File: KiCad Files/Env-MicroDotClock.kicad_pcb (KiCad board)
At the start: 2 copper layers, 90 x 65.2 mm, 40 parts, among them IC1 IS31FL3730-QFLS2-TR, IC2 IS31FL3730-QFLS2-TR, IC3 IS31FL3730-QFLS2-TR, IC4 IS31FL3730-QFLS2-TR, M1 Dip-14 Socket, M2 Dip-14 Socket, M3 Dip-14 Socket, M4 Dip-14 Socket, M5 Dip-14 Socket, M6 Dip-14 Socket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

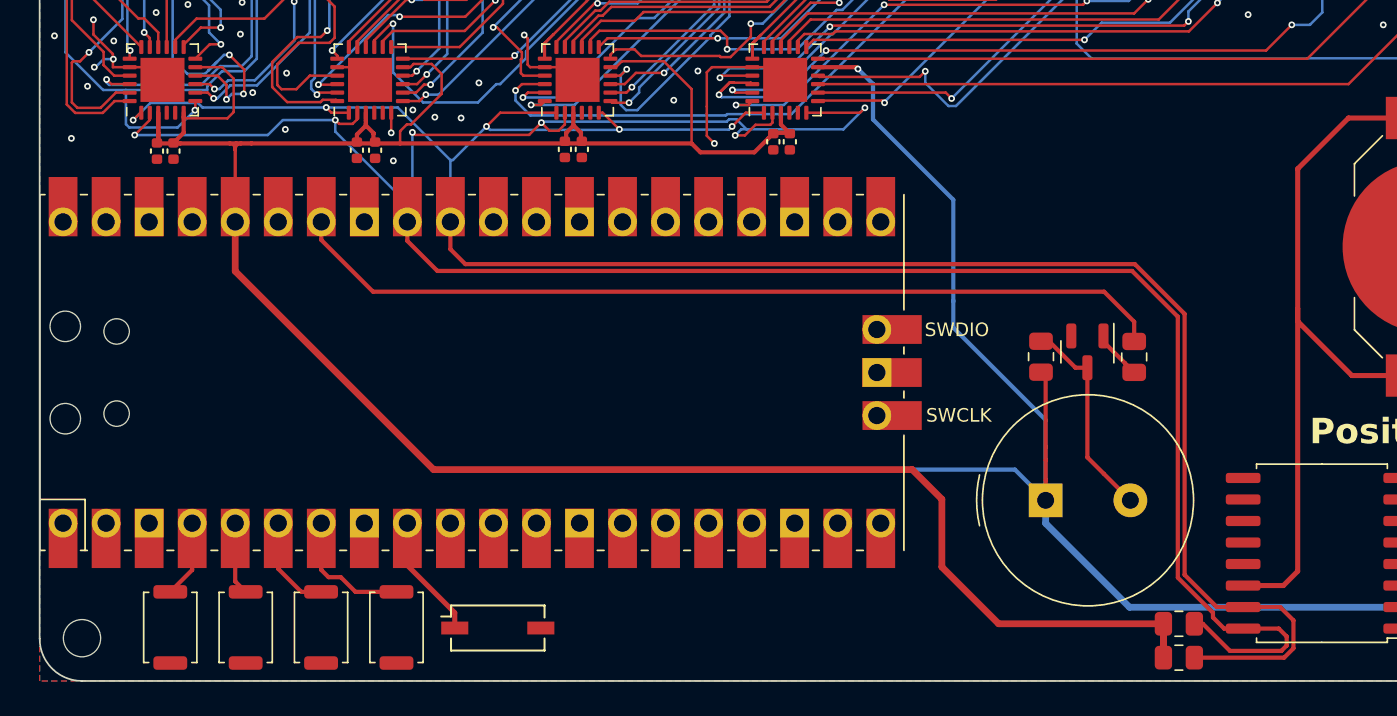
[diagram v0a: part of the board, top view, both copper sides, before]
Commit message: moved all i2c devices to dedicated gpio pairs, added individual pullups, ensured everything is 3.3V VCC or logic level 3V3 tied
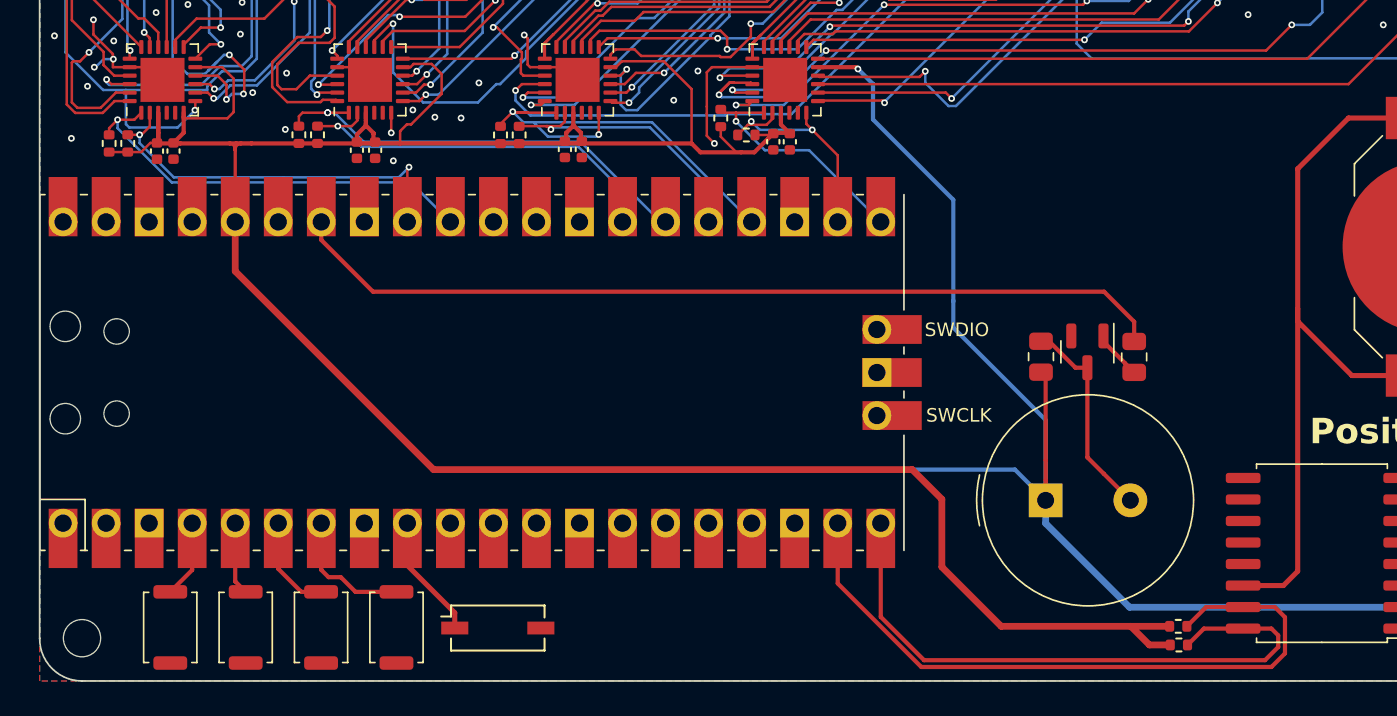
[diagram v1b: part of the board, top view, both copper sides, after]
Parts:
- added R10: 0402 10K, Resistor_SMD:R_0402_1005Metric, F.Cu at (90.2, 91.0)
- added R11: 0402 10K, Resistor_SMD:R_0402_1005Metric, F.Cu at (100.3, 90.5)
- added R12: 0402 10K, Resistor_SMD:R_0402_1005Metric, F.Cu at (101.4, 90.5)
- added R5: 0402 10K, Resistor_SMD:R_0402_1005Metric, F.Cu at (125.2, 89.5)
- added R6: 0402 10K, Resistor_SMD:R_0402_1005Metric, F.Cu at (126.7, 90.5)
- added R7: 0402 10K, Resistor_SMD:R_0402_1005Metric, F.Cu at (112.2, 90.5)
- added R8: 0402 10K, Resistor_SMD:R_0402_1005Metric, F.Cu at (113.3, 90.5)
- added R9: 0402 10K, Resistor_SMD:R_0402_1005Metric, F.Cu at (89.1, 91.0)
- R1, R2: value 0805 10K -> 0402 10K; footprint Resistor_SMD:R_0805_2012Metric -> Resistor_SMD:R_0402_1005Metric
- moved R2 1.85 mm to (152.2, 119.5)
- moved R1 1.25 mm to (152.2, 120.6)
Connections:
- IC1 pad 1: I2C_SDA -> I2C1_SDA
- IC1 pad 2: I2C_SCL -> I2C1_SCL
- IC2 pad 1: I2C_SDA -> I2C2_SDA
- IC2 pad 2: I2C_SCL -> I2C2_SCL
- IC3 pad 1: I2C_SDA -> I2C3_SDA
- IC3 pad 2: I2C_SCL -> I2C3_SCL
- IC3 pad 6: I2C_SDA -> I2C3_SDA
- IC4 pad 1: I2C_SDA -> I2C4_SDA
- IC4 pad 2: I2C_SCL -> I2C4_SCL
- IC4 pad 6: I2C_SCL -> I2C4_SCL
- R1 pad 2: I2C_SCL -> RTC_SCL
- R2 pad 2: I2C_SDA -> RTC_SDA
- U1 pad 19: unconnected-(U1-GPIO14-Pad19) -> RTC_SDA
- U1 pad 20: unconnected-(U1-GPIO15-Pad20) -> RTC_SCL
- U1 pad 21: unconnected-(U1-GPIO16-Pad21) -> I2C4_SDA
- U1 pad 22: unconnected-(U1-GPIO17-Pad22) -> I2C4_SCL
- U1 pad 24: unconnected-(U1-GPIO18-Pad24) -> I2C3_SDA
- U1 pad 25: unconnected-(U1-GPIO19-Pad25) -> I2C3_SCL
- U1 pad 26: unconnected-(U1-GPIO20-Pad26) -> I2C2_SDA
- U1 pad 27: unconnected-(U1-GPIO21-Pad27) -> I2C2_SCL
- U1 pad 31: I2C_SDA -> I2C1_SDA
- U1 pad 32: I2C_SCL -> I2C1_SCL
- U3 pad 15: I2C_SDA -> RTC_SDA
- U3 pad 16: I2C_SCL -> RTC_SCL
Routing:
- net I2C_SCL: track 145.0 -> 0.00 mm, vias 6 -> 0
- net I2C_SDA: track 131.3 -> 0.00 mm, vias 5 -> 0
- net RTC_SDA: track 0.00 -> 41.0 mm
- net RTC_SCL: track 0.00 -> 37.0 mm
- net I2C3_SDA: track 0.00 -> 27.0 mm, vias 0 -> 2
- net I2C2_SDA: track 0.00 -> 26.2 mm, vias 0 -> 2
- net I2C1_SDA: track 0.00 -> 25.1 mm, vias 0 -> 1
- net I2C2_SCL: track 0.00 -> 23.2 mm, vias 0 -> 1
- net I2C1_SCL: track 0.00 -> 23.1 mm, vias 0 -> 2
- net I2C3_SCL: track 0.00 -> 16.6 mm, vias 0 -> 1
- net I2C4_SDA: track 0.00 -> 14.1 mm, vias 0 -> 1
- net I2C4_SCL: track 0.00 -> 14.0 mm, vias 0 -> 2
- net +3V3: track 293.7 -> 298.9 mm

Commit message: changes toward a V2, replaced battery holder with larger one, moved rtc leftward to make space for larger battery.
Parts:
- removed SW5: DIP SPST W5.08mm_P1.27mm, Button_Switch_SMD:SW_DIP_SPSTx01_Slide_Copal_CHS-01A_W5.08mm_P1.27mm_JPin
- added REF**: KiCad-Logo2_6mm_SilkScreen, Symbol:KiCad-Logo2_6mm_SilkScreen, B.Cu at (124.0, 104.5)
- BT1: value HLD-012 -> Keystone 3034; footprint Battery:BatteryHolder_LINX_BAT-HLD-012-SMT -> Battery:BatteryHolder_Keystone_3034_1x20mm
- moved BZ1 17.3 mm to (147.0, 95.0), turned to 180 degrees
- moved C10 16.0 mm to (152.2, 117.9)
- moved C9 16.0 mm to (151.2, 117.9)
- moved R1 16.0 mm to (136.2, 120.6)
- moved R2 16.0 mm to (136.2, 119.5)
- moved U3 16.0 mm to (144.7, 115.2)
- moved BT1 8.47 mm to (161.8, 103.8)
- moved R4 7.83 mm to (141.8, 103.5), turned to 90 degrees
- moved R3 3.18 mm to (147.3, 103.5), turned to -90 degrees
- moved Q1 2.35 mm to (144.5, 103.8), turned to 90 degrees
- moved R6 1.51 mm to (125.2, 90.4), turned to 90 degrees
- moved R5 1.42 mm to (124.1, 90.4)
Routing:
- net +3V3: track 298.9 -> 271.5 mm, vias 2 -> 3
- net RTC_SCL: track 37.0 -> 22.3 mm
- net RTC_SDA: track 41.0 -> 26.7 mm
- net Net-(BT1-+): track 46.1 -> 55.7 mm
- net GPIO6: track 7.35 -> 0.00 mm
- net Buzzer GPIO: track 52.8 -> 46.9 mm
- net IC4C2: track 63.6 -> 65.7 mm
- net I2C4_SDA: track 14.1 -> 15.5 mm
- net I2C4_SCL: track 14.0 -> 14.9 mm
- net IC4C5: track 67.2 -> 66.4 mm
- net IC4R5: track 59.5 -> 60.1 mm
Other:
- board text added: "CR20XX"
- board text removed: "CR1220"

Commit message: small tweaks + generated production files
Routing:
- net IC3C5: track 52.3 -> 50.6 mm
- net Net-(BT1-+): track 55.7 -> 54.5 mm
- net Buzzer GPIO: track 46.9 -> 45.9 mm
- net IC4C5: track 66.4 -> 65.5 mm
- net I2C2_SDA: vias 2 -> 1
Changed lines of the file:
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@@
   (segment (start 139.2 72.845) (end 136.309 72.845) (width 0.15) (layer "F.Cu") (net 46))
   (segment (start 119 85.45) (end 120.1128 85.45) (width 0.15) (layer "F.Cu") (net 46))
-  (segment (start 118.6875 85.9999) (end 118.6875 86) (width 0.15) (layer "F.Cu") (net 46))
   (segment (start 136.309 72.845) (end 134.903 74.2513) (width 0.15) (layer "F.Cu") (net 46))
   (segment (start 120.1128 85.45) (end 120.5 85.8372) (width 0.15) (layer "F.Cu") (net 46))
@@
   (segment (start 138.810736 67.765) (end 139.2 67.765) (width 0.15) (layer "F.Cu") (net 53))
   (segment (start 149.595 72.845) (end 143.25 66.5) (width 0.15) (layer "F.Cu") (net 53))
-  (segment (start 114.8125 86) (end 114.8125 85.079218) (width 0.15) (layer "F.Cu") (net 53))
   (segment (start 116.933007 82.2129) (end 114.8125 84.333407) (width 0.15) (layer "F.Cu") (net 53))
   (segment (start 114.8125 84.333407) (end 114.8125 86) (width 0.15) (layer "F.Cu") (net 53))
   (segment (start 121.9476 82.2129) (end 116.933007 82.2129) (width 0.15) (layer "F.Cu") (net 53))
   (segment (start 143.25 66.5) (end 141.5658 66.5) (width 0.15) (layer "F.Cu") (net 53))
-  (segment (start 114.812 85.3097) (end 114.8125 85.3102) (width 0.15) (layer "F.Cu") (net 53))
   (segment (start 132.450736 74.125) (end 138.810736 67.765) (width 0.15) (layer "F.Cu") (net 53))
-  (segment (start 114.8125 85.3102) (end 114.8125 86) (width 0.15) (layer "F.Cu") (net 53))
   (segment (start 121.95 82.2153) (end 121.9476 82.2129) (width 0.15) (layer "F.Cu") (net 53))
   (segment (start 141.5658 66.5) (end 140.3008 67.765) (width 0.15) (layer "F.Cu") (net 53))
@@
   (segment (start 141.3205 82.2161) (end 141.6694 81.8672) (width 0.15) (layer "F.Cu") (net 71))
   (segment (start 150.337695 81.5612) (end 151.3888 81.5612) (width 0.15) (layer "F.Cu") (net 71))
-  (segment (start 127.0625 86) (end 127.0625 85.107006) (width 0.15) (layer "F.Cu") (net 71))
   (segment (start 153.5203 76.675) (end 158.5085 71.6868) (width 0.15) (layer "F.Cu") (net 71))
   (segment (start 160.7 67.765) (end 161.865 66.6) (width 0.15) (layer "F.Cu") (net 71))
@@
   (via (at 106.8 92.4) (size 0.4) (drill 0.2) (layers "F.Cu" "B.Cu") (net 84))
   (via (at 90.9 90.49) (size 0.4) (drill 0.2) (layers "F.Cu" "B.Cu") (net 84))
-  (segment (start 99.4 93) (end 92.924264 93) (width 0.15) (layer "B.Cu") (net 84))
+  (segment (start 92.924264 93) (end 106.2 93) (width 0.15) (layer "B.Cu") (net 84))
   (segment (start 106.2 93) (end 106.8 92.4) (width 0.15) (layer "B.Cu") (net 84))
   (segment (start 90.9 90.975736) (end 90.9 90.49) (width 0.15) (layer "B.Cu") (net 84))
-  (segment (start 99.4 93) (end 106.2 93) (width 0.15) (layer "B.Cu") (net 84))
   (segment (start 92.924264 93) (end 90.9 90.975736) (width 0.15) (layer "B.Cu") (net 84))
   (segment (start 100.5125 89.1875) (end 100.3 89.4) (width 0.15) (layer "F.Cu") (net 85))
   (segment (start 100.3 89.4) (end 100.3 89.98) (width 0.15) (layer "F.Cu") (net 85))
   (segment (start 103.25 89.1875) (end 100.5125 89.1875) (width 0.15) (layer "F.Cu") (net 85))
-  (via (at 102 89.1875) (size 0.4) (drill 0.2) (layers "F.Cu" "B.Cu") (net 85))
   (via (at 102 89.1875) (size 0.4) (drill 0.2) (layers "F.Cu" "B.Cu") (net 85))
   (segment (start 102.0125 89.2) (end 102 89.1875) (width 0.15) (layer "B.Cu") (net 85))
@@
   (segment (start 91.925 91) (end 92 91) (width 0.25) (layer "F.Cu") (net 95))
   (segment (start 104.25 89.8254) (end 104.25 89.65) (width 0.25) (layer "F.Cu") (net 95))
-  (segment (start 128.22 90.5) (end 128.3 90.42) (width 0.15) (layer "F.Cu") (net 95))
   (segment (start 128.0053 90.6997) (end 128.0203 90.6997) (width 0.15) (layer "F.Cu") (net 95))
   (segment (start 116.95 90.87) (end 116.95 91) (width 0.25) (layer "F.Cu") (net 95))
@@
   (segment (start 96.5424 95.631) (end 96.5424 91.375) (width 0.2) (layer "F.Cu") (net 95))
   (segment (start 92.9 90.97) (end 93.5 90.37) (width 0.25) (layer "F.Cu") (net 95))
-  (segment (start 146.9997 94.9999) (end 146.9997 94.9998) (width 0.15) (layer "F.Cu") (net 95))
   (segment (start 119.01 86.5) (end 119.36 86.1501) (width 0.15) (layer "F.Cu") (net 95))
   (segment (start 118.688 86.5) (end 119.01 86.5) (width 0.15) (layer "F.Cu") (net 95))
@@
   (segment (start 116.5 89.925) (end 116.95 90.375) (width 0.25) (layer "F.Cu") (net 95))
   (segment (start 93.5736 89.5187) (end 96.0813 89.5187) (width 0.15) (layer "F.Cu") (net 95))
-  (segment (start 135.7275 119.4625) (end 135.69 119.5) (width 0.4) (layer "F.Cu") (net 95))
   (segment (start 103.725 91) (end 104.7 91) (width 0.25) (layer "F.Cu") (net 95))
   (segment (start 106.275 90.275) (end 106.675 89.875) (width 0.15) (layer "F.Cu") (net 95))
@@
   (segment (start 135.69 118.81) (end 135.69 119.5) (width 0.4) (layer "F.Cu") (net 95))
   (segment (start 93.5 89.4451) (end 93.5 89.1875) (width 0.25) (layer "F.Cu") (net 95))
-  (segment (start 146.9997 94.9998) (end 146.9997 94.9999) (width 0.25) (layer "F.Cu") (net 95))
   (segment (start 124.1 90.91) (end 125.2 90.91) (width 0.25) (layer "F.Cu") (net 95))
   (segment (start 127.795 90.91) (end 128.0053 90.6997) (width 0.25) (layer "F.Cu") (net 95))
@@
   (segment (start 135.25 110.25) (end 108.2 110.25) (width 0.4) (layer "B.Cu") (net 95))
   (segment (start 144 112) (end 144 115.5) (width 0.6) (layer "F.Cu") (net 101))
-  (segment (start 151.25 98.25) (end 149.75 99.75) (width 0.6) (layer "F.Cu") (net 101))
-  (segment (start 144 115.5) (end 142.406 117.094) (width 0.6) (layer "F.Cu") (net 101))
+  (segment (start 149.75 99.75) (end 156.735 92.765) (width 0.6) (layer "F.Cu") (net 101))
+  (segment (start 142.406 117.094) (end 144 115.5) (width 0.6) (layer "F.Cu") (net 101))
   (segment (start 150.25 108.5) (end 156.485 114.735) (width 0.6) (layer "F.Cu") (net 101))
-  (segment (start 145.25 110.75) (end 144 112) (width 0.6) (layer "F.Cu") (net 101))
-  (segment (start 149.75 104.75) (end 149.75 106.25) (width 0.6) (layer "F.Cu") (net 101))
-  (segment (start 156.735 92.765) (end 151.25 98.25) (width 0.6) (layer "F.Cu") (net 101))
+  (segment (start 144 112) (end 147.5 108.5) (width 0.6) (layer "F.Cu") (net 101))
+  (segment (start 149.75 99.75) (end 149.75 106.25) (width 0.6) (layer "F.Cu") (net 101))
   (segment (start 149.75 106.25) (end 147.5 108.5) (width 0.6) (layer "F.Cu") (net 101))
   (segment (start 147.5 108.5) (end 150.25 108.5) (width 0.6) (layer "F.Cu") (net 101))
-  (segment (start 149.75 99.75) (end 149.75 104.75) (width 0.6) (layer "F.Cu") (net 101))
   (segment (start 142.406 117.094) (end 140.0304 117.094) (width 0.6) (layer "F.Cu") (net 101))
-  (segment (start 142.406 117.094) (end 143.25 116.25) (width 0.6) (layer "F.Cu") (net 101))
   (segment (start 156.485 114.735) (end 161.75 114.735) (width 0.6) (layer "F.Cu") (net 101))
-  (segment (start 147.5 108.5) (end 145.25 110.75) (width 0.6) (layer "F.Cu") (net 101))
   (segment (start 161.75 92.765) (end 156.735 92.765) (width 0.6) (layer "F.Cu") (net 101))
   (segment (start 142.0457 102.8228) (end 141.7737 102.5508) (width 0.25) (layer "F.Cu") (net 103))
@@
   (segment (start 143.5867 104.6956) (end 143.5867 104.6982) (width 0.15) (layer "F.Cu") (net 103))
   (segment (start 143.5867 104.6588) (end 143.5867 104.6798) (width 0.15) (layer "F.Cu") (net 103))
-  (segment (start 101.622 95.6643) (end 101.622 95.6476) (width 0.15) (layer "F.Cu") (net 104))
   (segment (start 101.622 95.6476) (end 101.622 95.631) (width 0.15) (layer "F.Cu") (net 104))
   (segment (start 131.5 99) (end 131 98.5) (width 0.4) (layer "F.Cu") (net 104))
-  (segment (start 101.622 95.8974) (end 101.622 95.7642) (width 0.15) (layer "F.Cu") (net 104))
   (segment (start 137 99) (end 131.5 99) (width 0.4) (layer "F.Cu") (net 104))
-  (segment (start 101.622 95.7642) (end 101.622 95.6976) (width 0.15) (layer "F.Cu") (net 104))
-  (segment (start 101.622 95.6643) (end 101.622 95.6476) (width 0.25) (layer "F.Cu") (net 104))
   (segment (start 101.622 95.6476) (end 101.622 95.631) (width 0.25) (layer "F.Cu") (net 104))
-  (segment (start 101.622 96.1642) (end 101.622 96.1638) (width 0.15) (layer "F.Cu") (net 104))
   (segment (start 102.5 98.5) (end 101.6224 97.6224) (width 0.4) (layer "F.Cu") (net 104))
   (segment (start 101.6224 97.6224) (end 101.6224 95.631) (width 0.4) (layer "F.Cu") (net 104))
-  (segment (start 101.622 96.1642) (end 101.622 96.1638) (width 0.25) (layer "F.Cu") (net 104))
   (segment (start 139 102.5) (end 139 101) (width 0.4) (layer "F.Cu") (net 104))
   (segment (start 101.622 95.6476) (end 101.6224 95.6472) (width 0.15) (layer "F.Cu") (net 104))
   (segment (start 140.8753 104.3753) (end 139 102.5) (width 0.4) (layer "F.Cu") (net 104))
-  (segment (start 101.622 95.7642) (end 101.622 95.6976) (width 0.25) (layer "F.Cu") (net 104))
   (segment (start 131 98.5) (end 102.5 98.5) (width 0.4) (layer "F.Cu") (net 104))
-  (segment (start 101.622 95.6976) (end 101.622 95.6643) (width 0.15) (layer "F.Cu") (net 104))
-  (segment (start 101.622 95.8974) (end 101.622 95.7642) (width 0.25) (layer "F.Cu") (net 104))
-  (segment (start 101.622 96.1638) (end 101.622 95.8974) (width 0.15) (layer "F.Cu") (net 104))
   (segment (start 141.7737 104.3753) (end 140.8753 104.3753) (width 0.4) (layer "F.Cu") (net 104))
-  (segment (start 101.622 96.1638) (end 101.622 95.8974) (width 0.25) (layer "F.Cu") (net 104))
   (segment (start 139 101) (end 137 99) (width 0.4) (layer "F.Cu") (net 104))
-  (segment (start 101.622 95.6976) (end 101.622 95.6643) (width 0.25) (layer "F.Cu") (net 104))
   (segment (start 101.6224 95.6472) (end 101.6224 95.631) (width 0.15) (layer "F.Cu") (net 104))
   (segment (start 142.5 118.964) (end 142.5 121.1) (width 0.25) (layer "F.Cu") (net 105))

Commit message: removed all traces for work on future version
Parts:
- removed REF**: KiCad-Logo2_6mm_SilkScreen, Symbol:KiCad-Logo2_6mm_SilkScreen
- IC1, IC2, IC3, IC4: footprint Package_DFN_QFN:QFN-24-1EP_4x4mm_P0.5mm_EP2.6x2.6mm -> Package_DFN_QFN:QFN-24-1EP_4x4mm_P0.5mm_EP2.6x2.6mm_ThermalVias
- moved R5 9.80 mm to (131.2, 83.6), turned to -90 degrees
- moved R7 9.71 mm to (118.9, 83.5), turned to -90 degrees
- moved R11 9.39 mm to (106.7, 83.6), turned to -90 degrees
- moved R9 9.09 mm to (94.3, 83.5), turned to -90 degrees
- moved R6 8.36 mm to (130.1, 83.6), turned to -90 degrees
- moved R8 8.34 mm to (117.8, 83.5), turned to -90 degrees
- moved R12 8.06 mm to (105.5, 83.6), turned to -90 degrees
- moved R10 8.03 mm to (93.2, 83.5), turned to -90 degrees
- moved C2 5.80 mm to (87.7, 89.0), turned to 180 degrees
- moved C1 5.49 mm to (87.7, 88.0), turned to 180 degrees
- moved C4 5.15 mm to (100.2, 89.1), turned to 180 degrees
- moved C6 5.13 mm to (112.4, 89.0), turned to 180 degrees
- moved C8 4.99 mm to (124.7, 89.0), turned to 180 degrees
- moved C3 4.90 mm to (100.2, 88.0), turned to 180 degrees
- moved C5 4.88 mm to (112.4, 88.0), turned to 180 degrees
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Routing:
- net +3V3: track 271.3 -> 0.00 mm, vias 3 -> 0
- net IC4R3: track 66.2 -> 0.00 mm
- net IC4C2: track 65.7 -> 0.00 mm, vias 1 -> 0
- net IC4C5: track 65.5 -> 0.00 mm
- net IC3C6: track 60.6 -> 0.00 mm, vias 4 -> 0
- net IC3C2: track 60.1 -> 0.00 mm, vias 4 -> 0
- net IC4C7: track 60.1 -> 0.00 mm, vias 3 -> 0
- net IC4R5: track 60.1 -> 0.00 mm, vias 1 -> 0
- net IC4C4: track 59.1 -> 0.00 mm, vias 5 -> 0
- net IC4C3: track 58.1 -> 0.00 mm, vias 5 -> 0
- net IC4C1: track 58.1 -> 0.00 mm, vias 3 -> 0
- net IC3R4: track 57.1 -> 0.00 mm, vias 1 -> 0
- net IC3C4: track 55.2 -> 0.00 mm, vias 8 -> 0
- net Net-(BT1-+): track 54.5 -> 0.00 mm
- net IC4R4: track 54.3 -> 0.00 mm, vias 2 -> 0
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
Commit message: Kicad Verion
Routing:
- net +3V3: track 0.00 -> 236.2 mm, vias 0 -> 4
- net IC4R5: track 0.00 -> 91.4 mm, vias 0 -> 1
- net IC4R3: track 0.00 -> 78.8 mm, vias 0 -> 4
- net IC4R4: track 0.00 -> 76.3 mm, vias 0 -> 2
- net IC3R3: track 0.00 -> 73.6 mm, vias 0 -> 4
- net IC4R2: track 0.00 -> 71.4 mm, vias 0 -> 5
- net IC1C2: track 0.00 -> 70.8 mm, vias 0 -> 1
- net IC3C5: track 0.00 -> 67.5 mm, vias 0 -> 4
- net IC4C2: track 0.00 -> 67.2 mm, vias 0 -> 1
- net IC4C5: track 0.00 -> 67.0 mm, vias 0 -> 1
- net IC3R2: track 0.00 -> 65.6 mm, vias 0 -> 4
- net Net-(BT1-+): track 0.00 -> 63.7 mm
- net IC2R5: track 0.00 -> 63.2 mm, vias 0 -> 7
- net IC4R1: track 0.00 -> 62.7 mm, vias 0 -> 3
- net IC3R4: track 0.00 -> 62.7 mm, vias 0 -> 4
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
